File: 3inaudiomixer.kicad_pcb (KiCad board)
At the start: 2 copper layers, 64 x 65 mm, 40 parts, among them J1 AudioJack3, J2 AudioJack3, J3 AudioJack3, J4 AudioJack3, U1 LF353D, U2 LF353D, U3 L78L05_SOT89, U4 L79L05_SOT89

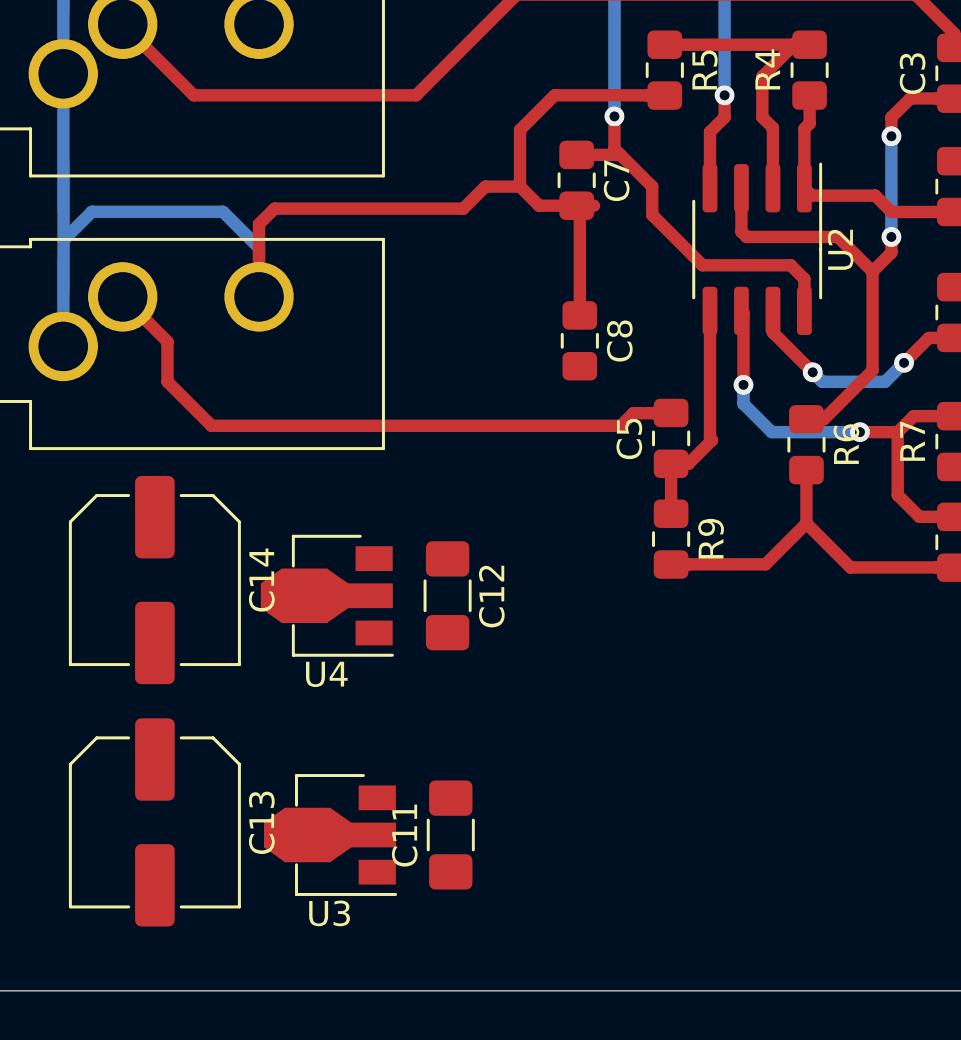
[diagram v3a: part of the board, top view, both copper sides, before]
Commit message: all traces routed, beta board
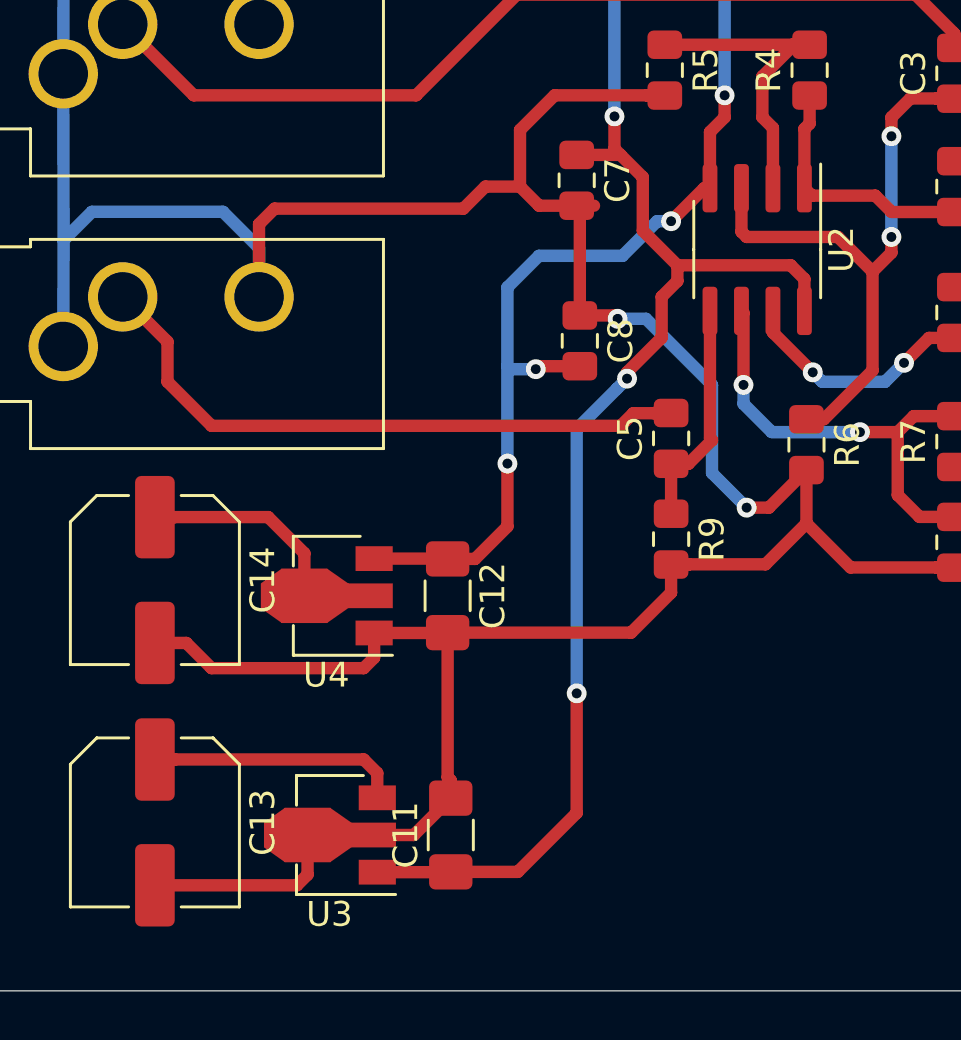
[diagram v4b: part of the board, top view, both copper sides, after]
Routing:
- net Net-(C10-Pad1): track 247.0 -> 308.7 mm, vias 4 -> 6
- net Net-(C11-Pad1): track 53.0 -> 86.4 mm, vias 4 -> 6
- net Net-(C10-Pad2): track 49.0 -> 77.5 mm, vias 4 -> 7
- net Net-(C14-Pad1): track 0.00 -> 12.4 mm
- net Net-(C13-Pad1): track 0.00 -> 10.2 mm
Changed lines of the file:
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@@
     (thickness 1.6)
     (drawings 4)
-    (tracks 330)
+    (tracks 405)
     (zones 0)
     (modules 40)
@@
   (segment (start 151.765 97.917) (end 149.987 96.139) (width 0.5) (layer F.Cu) (net 13))
   (segment (start 155.247 97.917) (end 151.765 97.917) (width 0.5) (layer F.Cu) (net 13))
+  (segment (start 132.544 101.56) (end 132.544 100.56) (width 0.5) (layer F.Cu) (net 13))
+  (segment (start 132.123 101.981) (end 132.544 101.56) (width 0.5) (layer F.Cu) (net 13))
+  (segment (start 125.984 101.981) (end 132.123 101.981) (width 0.5) (layer F.Cu) (net 13))
+  (segment (start 124.9655 100.9625) (end 125.984 101.981) (width 0.5) (layer F.Cu) (net 13))
+  (segment (start 123.698 100.9625) (end 124.9655 100.9625) (width 0.5) (layer F.Cu) (net 13))
+  (segment (start 135.4965 100.56) (end 135.509 100.5475) (width 0.5) (layer F.Cu) (net 13))
+  (segment (start 132.544 100.56) (end 135.4965 100.56) (width 0.5) (layer F.Cu) (net 13))
+  (segment (start 129.8575 110.312) (end 129.8575 108.712) (width 0.5) (layer F.Cu) (net 13))
+  (segment (start 129.428 110.7415) (end 129.8575 110.312) (width 0.5) (layer F.Cu) (net 13))
+  (segment (start 123.698 110.7415) (end 129.428 110.7415) (width 0.5) (layer F.Cu) (net 13))
+  (segment (start 134.1485 108.712) (end 135.636 107.2245) (width 0.5) (layer F.Cu) (net 13))
+  (segment (start 132.5245 108.712) (end 134.1485 108.712) (width 0.5) (layer F.Cu) (net 13))
+  (segment (start 135.636 107.2245) (end 135.636 106.512) (width 0.5) (layer F.Cu) (net 13))
+  (segment (start 135.509 106.385) (end 135.509 100.5475) (width 0.5) (layer F.Cu) (net 13))
+  (segment (start 135.636 106.512) (end 135.509 106.385) (width 0.5) (layer F.Cu) (net 13))
+  (segment (start 128.524 108.712) (end 132.5245 108.712) (width 0.5) (layer F.Cu) (net 13))
+  (via (at 142.367 87.884) (size 0.8) (drill 0.4) (layers F.Cu B.Cu) (net 13))
+  (segment (start 142.231 87.748) (end 142.367 87.884) (width 0.5) (layer F.Cu) (net 13))
+  (segment (start 140.843 87.748) (end 142.231 87.748) (width 0.5) (layer F.Cu) (net 13))
+  (via (at 147.574 95.504) (size 0.8) (drill 0.4) (layers F.Cu B.Cu) (net 13))
+  (segment (start 148.472 95.504) (end 149.987 93.989) (width 0.5) (layer F.Cu) (net 13))
+  (segment (start 147.574 95.504) (end 148.472 95.504) (width 0.5) (layer F.Cu) (net 13))
+  (segment (start 146.177 94.107) (end 147.574 95.504) (width 0.5) (layer B.Cu) (net 13))
+  (segment (start 146.177 90.551) (end 146.177 94.107) (width 0.5) (layer B.Cu) (net 13))
+  (segment (start 143.51 87.884) (end 146.177 90.551) (width 0.5) (layer B.Cu) (net 13))
+  (segment (start 142.367 87.884) (end 143.51 87.884) (width 0.5) (layer B.Cu) (net 13))
+  (segment (start 135.509 100.5475) (end 142.9115 100.5475) (width 0.5) (layer F.Cu) (net 13))
+  (segment (start 144.526 98.933) (end 144.526 97.799) (width 0.5) (layer F.Cu) (net 13))
+  (segment (start 142.9115 100.5475) (end 144.526 98.933) (width 0.5) (layer F.Cu) (net 13))
   (segment (start 140.716 81.271) (end 142.485 81.271) (width 0.5) (layer F.Cu) (net 14))
-  (segment (start 142.485 81.271) (end 143.764 82.55) (width 0.5) (layer F.Cu) (net 14))
-  (segment (start 143.764 82.55) (end 143.764 83.693) (width 0.5) (layer F.Cu) (net 14))
-  (segment (start 143.764 83.693) (end 145.796 85.725) (width 0.5) (layer F.Cu) (net 14))
-  (segment (start 145.796 85.725) (end 149.352 85.725) (width 0.5) (layer F.Cu) (net 14))
-  (segment (start 149.905 86.278) (end 149.905 87.565) (width 0.5) (layer F.Cu) (net 14))
-  (segment (start 149.352 85.725) (end 149.905 86.278) (width 0.5) (layer F.Cu) (net 14))
   (segment (start 155.439 68.97) (end 157.48 66.929) (width 0.5) (layer F.Cu) (net 14))
   (segment (start 157.48 66.929) (end 157.48 63.5) (width 0.5) (layer F.Cu) (net 14))
@@
   (segment (start 142.24 81.026) (end 142.485 81.271) (width 0.5) (layer F.Cu) (net 14))
   (segment (start 142.24 79.717) (end 142.24 81.026) (width 0.5) (layer F.Cu) (net 14))
+  (segment (start 135.6235 110.212) (end 135.636 110.1995) (width 0.5) (layer F.Cu) (net 14))
+  (segment (start 132.671 110.212) (end 135.6235 110.212) (width 0.5) (layer F.Cu) (net 14))
+  (segment (start 149.905 86.278) (end 149.905 87.565) (width 0.5) (layer F.Cu) (net 14))
+  (segment (start 149.352 85.725) (end 149.905 86.278) (width 0.5) (layer F.Cu) (net 14))
+  (segment (start 144.78 85.725) (end 149.352 85.725) (width 0.5) (layer F.Cu) (net 14))
+  (segment (start 143.383 84.328) (end 144.78 85.725) (width 0.5) (layer F.Cu) (net 14))
+  (segment (start 143.383 82.169) (end 143.383 84.328) (width 0.5) (layer F.Cu) (net 14))
+  (segment (start 142.485 81.271) (end 143.383 82.169) (width 0.5) (layer F.Cu) (net 14))
+  (via (at 142.748 90.297) (size 0.8) (drill 0.4) (layers F.Cu B.Cu) (net 14))
+  (segment (start 142.748 90.297) (end 142.348001 90.696999) (width 0.5) (layer B.Cu) (net 14))
+  (segment (start 140.716 92.329) (end 140.716 102.997) (width 0.5) (layer B.Cu) (net 14))
+  (via (at 140.716 102.997) (size 0.8) (drill 0.4) (layers F.Cu B.Cu) (net 14))
+  (segment (start 142.348001 90.696999) (end 140.716 92.329) (width 0.5) (layer B.Cu) (net 14))
+  (segment (start 140.716 102.997) (end 140.716 107.823) (width 0.5) (layer F.Cu) (net 14))
+  (segment (start 138.3395 110.1995) (end 135.636 110.1995) (width 0.5) (layer F.Cu) (net 14))
+  (segment (start 140.716 107.823) (end 138.3395 110.1995) (width 0.5) (layer F.Cu) (net 14))
+  (segment (start 142.748 90.043) (end 142.748 90.297) (width 0.5) (layer F.Cu) (net 14))
+  (segment (start 144.145 88.646) (end 142.748 90.043) (width 0.5) (layer F.Cu) (net 14))
+  (segment (start 144.145 86.995) (end 144.145 88.646) (width 0.5) (layer F.Cu) (net 14))
+  (segment (start 144.78 86.36) (end 144.145 86.995) (width 0.5) (layer F.Cu) (net 14))
+  (segment (start 144.78 85.725) (end 144.78 86.36) (width 0.5) (layer F.Cu) (net 14))
   (via (at 158.242 56.007) (size 0.8) (drill 0.4) (layers F.Cu B.Cu) (net 15))
   (segment (start 159.639 54.61) (end 158.242 56.007) (width 0.5) (layer F.Cu) (net 15))
@@
   (segment (start 142.748 59.055) (end 143.764 58.039) (width 0.5) (layer F.Cu) (net 15))
   (segment (start 142.748 60.579) (end 142.748 59.055) (width 0.5) (layer F.Cu) (net 15))
+  (segment (start 135.4965 97.56) (end 135.509 97.5725) (width 0.5) (layer F.Cu) (net 15))
+  (segment (start 132.544 97.56) (end 135.4965 97.56) (width 0.5) (layer F.Cu) (net 15))
+  (via (at 144.526 83.947) (size 0.8) (drill 0.4) (layers F.Cu B.Cu) (net 15))
+  (segment (start 145.858 82.615) (end 144.526 83.947) (width 0.5) (layer F.Cu) (net 15))
+  (segment (start 146.095 82.615) (end 145.858 82.615) (width 0.5) (layer F.Cu) (net 15))
+  (segment (start 143.960315 83.947) (end 142.563315 85.344) (width 0.5) (layer B.Cu) (net 15))
+  (segment (start 144.526 83.947) (end 143.960315 83.947) (width 0.5) (layer B.Cu) (net 15))
+  (segment (start 142.563315 85.344) (end 139.192 85.344) (width 0.5) (layer B.Cu) (net 15))
+  (via (at 137.922 93.726) (size 0.8) (drill 0.4) (layers F.Cu B.Cu) (net 15))
+  (segment (start 139.192 85.344) (end 137.922 86.614) (width 0.5) (layer B.Cu) (net 15))
+  (segment (start 137.922 93.726) (end 137.922 96.266) (width 0.5) (layer F.Cu) (net 15))
+  (segment (start 136.6155 97.5725) (end 135.509 97.5725) (width 0.5) (layer F.Cu) (net 15))
+  (segment (start 137.922 96.266) (end 136.6155 97.5725) (width 0.5) (layer F.Cu) (net 15))
+  (via (at 139.065 89.916) (size 0.8) (drill 0.4) (layers F.Cu B.Cu) (net 15))
+  (segment (start 139.183 89.798) (end 139.065 89.916) (width 0.5) (layer F.Cu) (net 15))
+  (segment (start 140.843 89.798) (end 139.183 89.798) (width 0.5) (layer F.Cu) (net 15))
+  (segment (start 138.049 89.916) (end 137.922 89.789) (width 0.5) (layer B.Cu) (net 15))
+  (segment (start 139.065 89.916) (end 138.049 89.916) (width 0.5) (layer B.Cu) (net 15))
+  (segment (start 137.922 89.789) (end 137.922 93.726) (width 0.5) (layer B.Cu) (net 15))
+  (segment (start 137.922 86.614) (end 137.922 89.789) (width 0.5) (layer B.Cu) (net 15))
+  (segment (start 124.498 105.6665) (end 124.5005 105.664) (width 0.5) (layer F.Cu) (net 16))
+  (segment (start 123.698 105.6665) (end 124.498 105.6665) (width 0.5) (layer F.Cu) (net 16))
+  (segment (start 132.671 106.212) (end 132.671 107.212) (width 0.5) (layer F.Cu) (net 16))
+  (segment (start 132.123 105.664) (end 132.671 106.212) (width 0.5) (layer F.Cu) (net 16))
+  (segment (start 124.5005 105.664) (end 132.123 105.664) (width 0.5) (layer F.Cu) (net 16))
+  (segment (start 124.498 95.8875) (end 124.5005 95.885) (width 0.5) (layer F.Cu) (net 17))
+  (segment (start 123.698 95.8875) (end 124.498 95.8875) (width 0.5) (layer F.Cu) (net 17))
+  (segment (start 124.5005 95.885) (end 128.27 95.885) (width 0.5) (layer F.Cu) (net 17))
+  (segment (start 129.7305 97.3455) (end 129.7305 99.06) (width 0.5) (layer F.Cu) (net 17))
+  (segment (start 128.27 95.885) (end 129.7305 97.3455) (width 0.5) (layer F.Cu) (net 17))
+  (segment (start 128.397 99.06) (end 132.3975 99.06) (width 0.5) (layer F.Cu) (net 17))
   (segment (start 155.002 52.061) (end 154.993 52.07) (width 0.5) (layer F.Cu) (net 18))
   (segment (start 155.702 52.061) (end 155.002 52.061) (width 0.5) (layer F.Cu) (net 18))

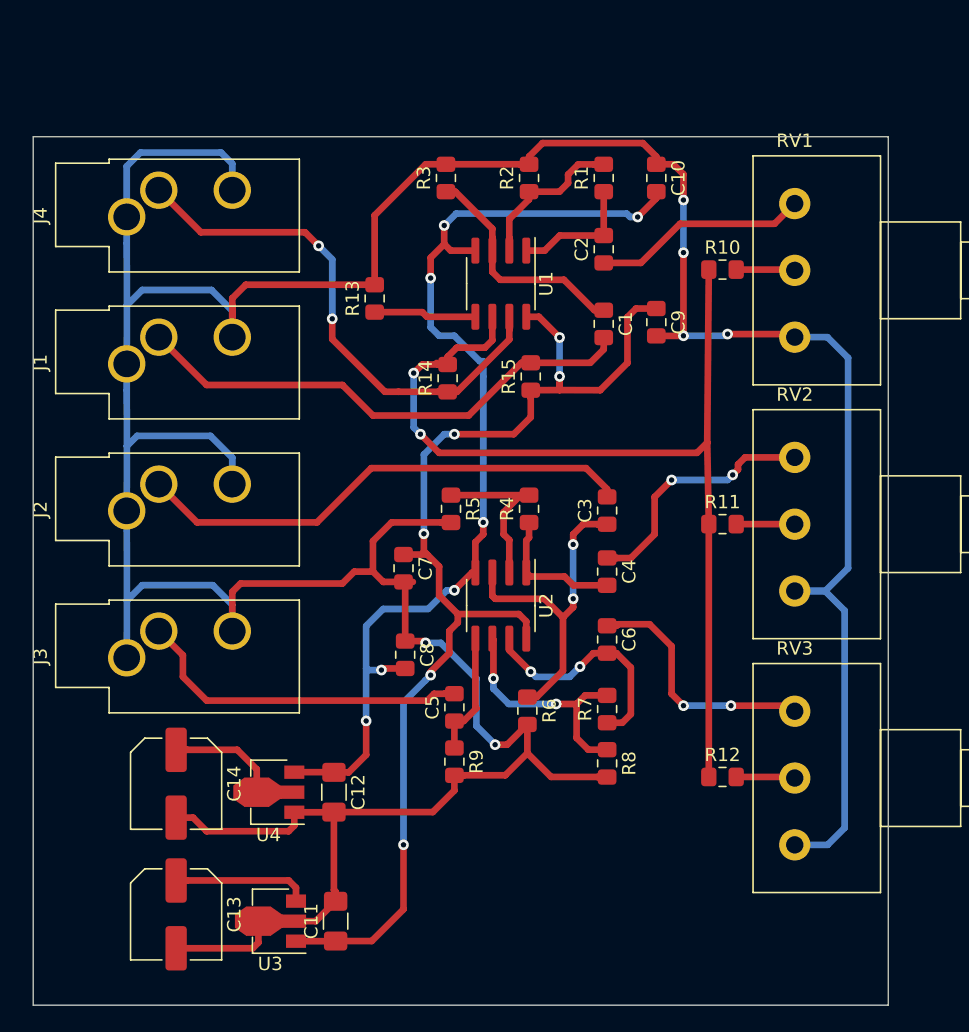
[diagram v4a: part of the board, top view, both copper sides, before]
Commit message: mounting holes
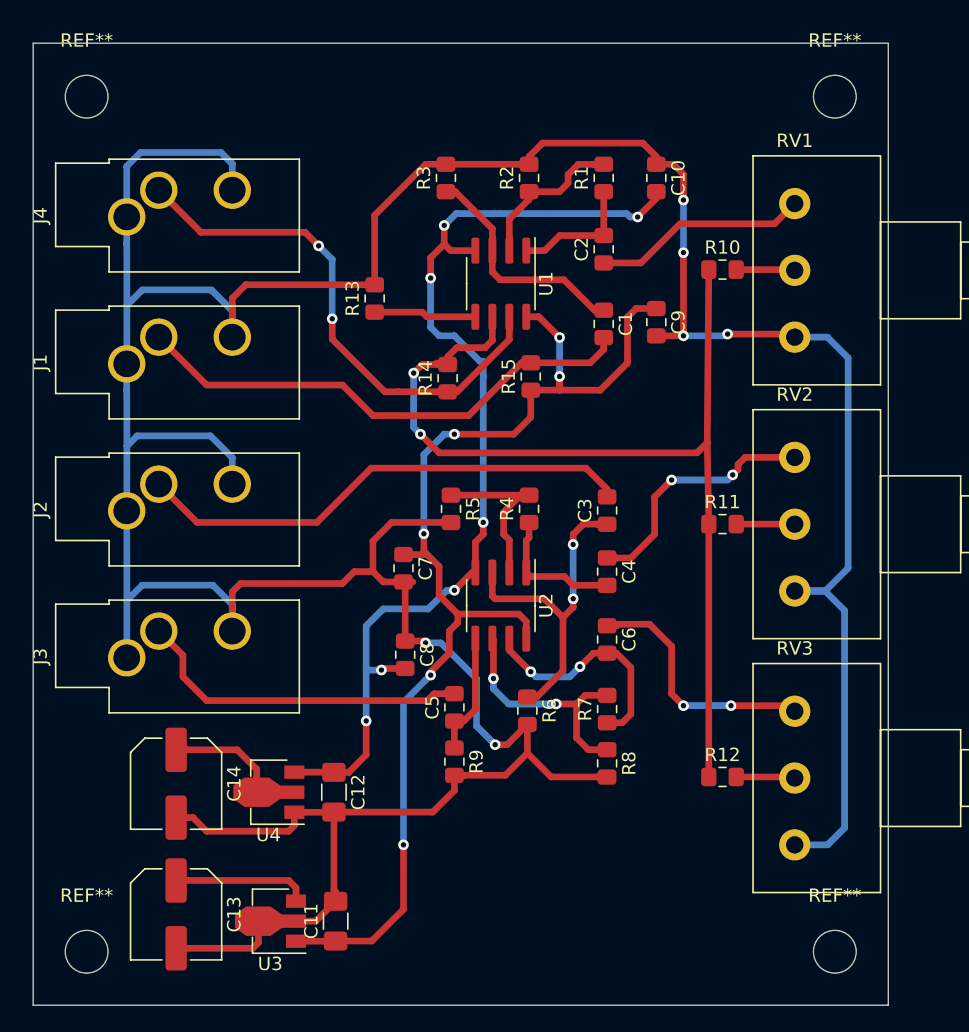
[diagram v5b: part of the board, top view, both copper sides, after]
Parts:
- added REF**: MountingHole_3.2mm_M3, MountingHole:MountingHole_3.2mm_M3, F.Cu at (117.0, 111.0)
- added REF**: MountingHole_3.2mm_M3, MountingHole:MountingHole_3.2mm_M3, F.Cu at (173.0, 111.0)
- added REF**: MountingHole_3.2mm_M3, MountingHole:MountingHole_3.2mm_M3, F.Cu at (117.0, 47.0)
- added REF**: MountingHole_3.2mm_M3, MountingHole:MountingHole_3.2mm_M3, F.Cu at (173.0, 47.0)
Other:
- board size 64 x 65 mm -> 64 x 72 mm
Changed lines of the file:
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@@
     (tracks 405)
     (zones 0)
-    (modules 40)
+    (modules 44)
     (nets 27)
   )
@@
     (add_net "Net-(R7-Pad2)")
   )
+  (module MountingHole:MountingHole_3.2mm_M3 (layer F.Cu)
+    (at 117 111)
+    (descr "Mounting Hole 3.2mm, no annular, M3")
+    (tags "mounting hole 3.2mm no annular m3")
+    (attr virtual)
+    (fp_text reference REF** (at 0 -4.2) (layer F.SilkS)
+      (effects (font (size 1 1) (thickness 0.15)))
+    )
+    (fp_text value MountingHole_3.2mm_M3 (at 0 4.2) (layer F.Fab)
+      (effects (font (size 1 1) (thickness 0.15)))
+    )
+    (fp_circle (center 0 0) (end 3.45 0) (layer F.CrtYd) (width 0.05))
+    (fp_circle (center 0 0) (end 3.2 0) (layer Cmts.User) (width 0.15))
+    (fp_text user %R (at 0.3 0) (layer F.Fab)
+      (effects (font (size 1 1) (thickness 0.15)))
+    )
+    (pad 1 np_thru_hole circle (at 0 0) (size 3.2 3.2) (drill 3.2) (layers *.Cu *.Mask))
+  )
+  (module MountingHole:MountingHole_3.2mm_M3 (layer F.Cu)
+    (at 173 111)
+    (descr "Mounting Hole 3.2mm, no annular, M3")
+    (tags "mounting hole 3.2mm no annular m3")
+    (attr virtual)
+    (fp_text reference REF** (at 0 -4.2) (layer F.SilkS)
+      (effects (font (size 1 1) (thickness 0.15)))
+    )
+    (fp_text value MountingHole_3.2mm_M3 (at 0 4.2) (layer F.Fab)
+      (effects (font (size 1 1) (thickness 0.15)))
+    )
+    (fp_circle (center 0 0) (end 3.45 0) (layer F.CrtYd) (width 0.05))
+    (fp_circle (center 0 0) (end 3.2 0) (layer Cmts.User) (width 0.15))
+    (fp_text user %R (at 0.3 0) (layer F.Fab)
+      (effects (font (size 1 1) (thickness 0.15)))
+    )
+    (pad 1 np_thru_hole circle (at 0 0) (size 3.2 3.2) (drill 3.2) (layers *.Cu *.Mask))
+  )
+  (module MountingHole:MountingHole_3.2mm_M3 (layer F.Cu)
+    (at 117 47)
+    (descr "Mounting Hole 3.2mm, no annular, M3")
+    (tags "mounting hole 3.2mm no annular m3")
+    (attr virtual)
+    (fp_text reference REF** (at 0 -4.2) (layer F.SilkS)
+      (effects (font (size 1 1) (thickness 0.15)))
+    )
+    (fp_text value MountingHole_3.2mm_M3 (at 0 4.2) (layer F.Fab)
+      (effects (font (size 1 1) (thickness 0.15)))
+    )
+    (fp_circle (center 0 0) (end 3.45 0) (layer F.CrtYd) (width 0.05))
+    (fp_circle (center 0 0) (end 3.2 0) (layer Cmts.User) (width 0.15))
+    (fp_text user %R (at 0.3 0) (layer F.Fab)
+      (effects (font (size 1 1) (thickness 0.15)))
+    )
+    (pad 1 np_thru_hole circle (at 0 0) (size 3.2 3.2) (drill 3.2) (layers *.Cu *.Mask))
+  )
+  (module MountingHole:MountingHole_3.2mm_M3 (layer F.Cu)
+    (at 173 47)
+    (descr "Mounting Hole 3.2mm, no annular, M3")
+    (tags "mounting hole 3.2mm no annular m3")
+    (attr virtual)
+    (fp_text reference REF** (at 0 -4.2) (layer F.SilkS)
+      (effects (font (size 1 1) (thickness 0.15)))
+    )
+    (fp_text value MountingHole_3.2mm_M3 (at 0 4.2) (layer F.Fab)
+      (effects (font (size 1 1) (thickness 0.15)))
+    )
+    (fp_circle (center 0 0) (end 3.45 0) (layer F.CrtYd) (width 0.05))
+    (fp_circle (center 0 0) (end 3.2 0) (layer Cmts.User) (width 0.15))
+    (fp_text user %R (at 0.3 0) (layer F.Fab)
+      (effects (font (size 1 1) (thickness 0.15)))
+    )
+    (pad 1 np_thru_hole circle (at 0 0) (size 3.2 3.2) (drill 3.2) (layers *.Cu *.Mask))
+  )
   (module Connector_Audio:Jack_3.5mm_CUI_SJ1-3533NG_Horizontal_CircularHoles (layer F.Cu)
     (at 120 56 90)
@@
     )
   )
-  (gr_line (start 113 50) (end 113 115) (layer Edge.Cuts) (width 0.05))
-  (gr_line (start 177 50) (end 177 115) (layer Edge.Cuts) (width 0.05))
+  (gr_line (start 113 43) (end 113 115) (layer Edge.Cuts) (width 0.05))
+  (gr_line (start 177 43) (end 177 115) (layer Edge.Cuts) (width 0.05))
   (gr_line (start 113 115) (end 177 115) (layer Edge.Cuts) (width 0.05))
-  (gr_line (start 113 50) (end 177 50) (layer Edge.Cuts) (width 0.05))
+  (gr_line (start 113 43) (end 177 43) (layer Edge.Cuts) (width 0.05))
   (segment (start 150.241 66.92) (end 154.695 66.92) (width 0.5) (layer F.Cu) (net 1))
   (segment (start 155.702 65.913) (end 155.702 65.033) (width 0.5) (layer F.Cu) (net 1))
